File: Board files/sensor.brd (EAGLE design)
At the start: 25.4 x 59.7 mm, 32 parts, among them Q1 BCM847DS, U1 TL974, U2 TL974

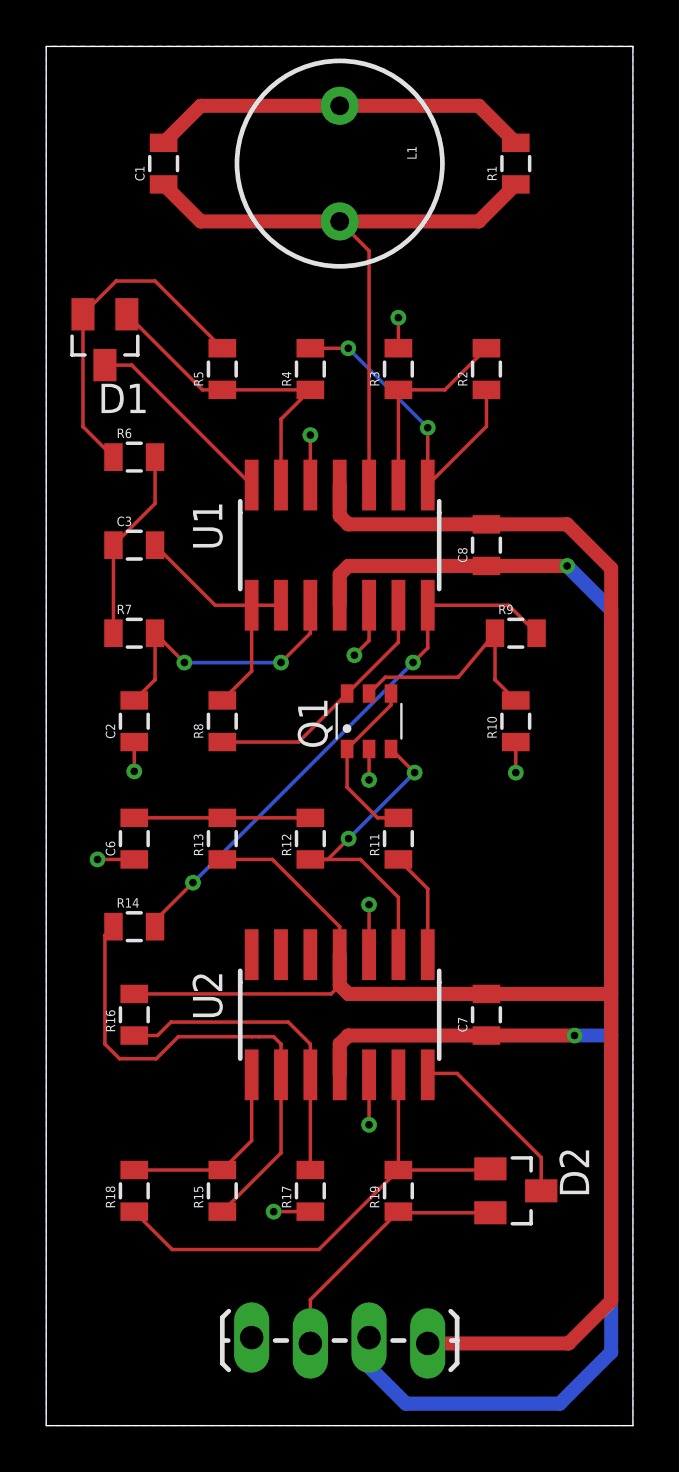
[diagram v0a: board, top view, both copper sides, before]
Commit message: Added component values and removed final rectifier
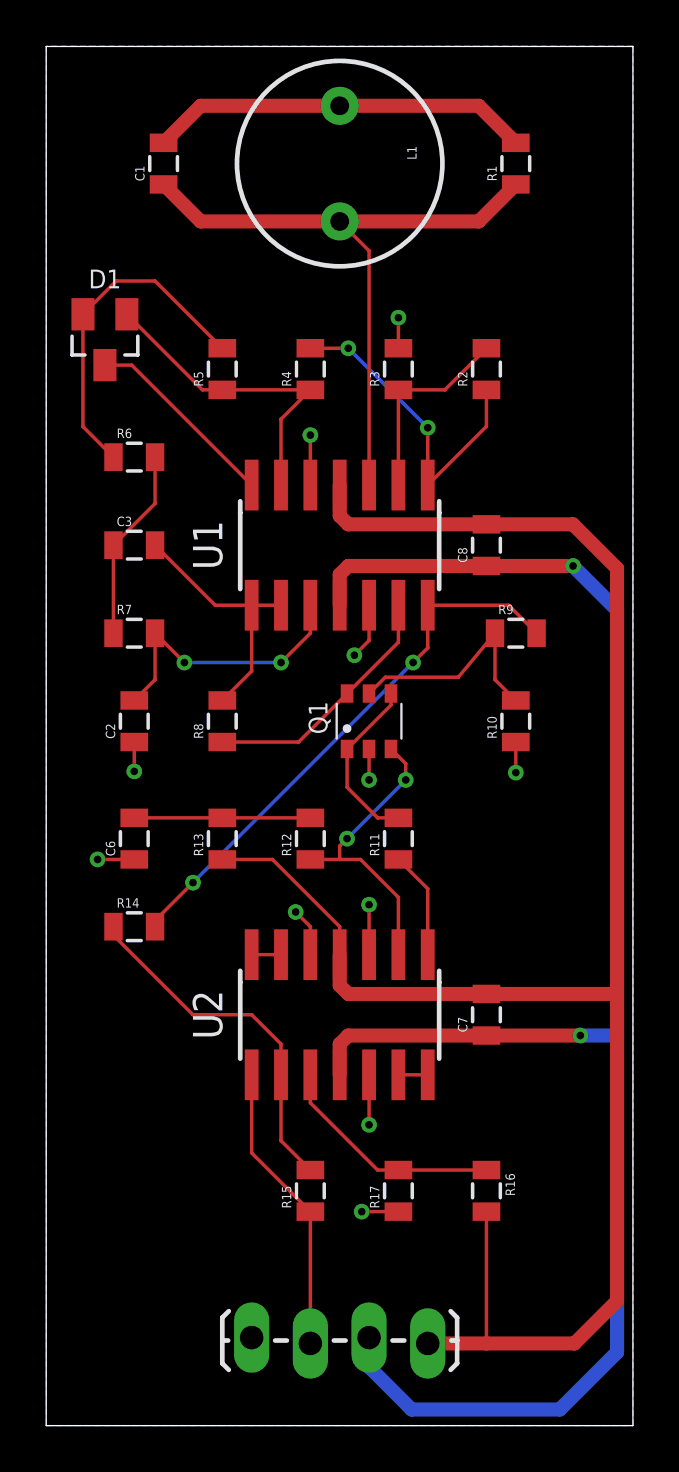
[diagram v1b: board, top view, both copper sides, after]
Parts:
- removed D2: BAS70-04, diode:SOT23
- removed R18, R19: (no value), SparkFun-Resistors:0805
- C1: value (none) -> 4.7nF
- C6: value (none) -> 0.1uF
- L1: value (none) -> 1mH
- R1, R10: value (none) -> 1K
- R11: value (none) -> 2K
- R12, R13: value (none) -> 499K
- R14, R17, R3, R4, R5, R8: value (none) -> 10K
- R15, R2: value (none) -> 68K
- R16: value (none) -> 40.2K
- R9: value (none) -> 15K
- moved R16 17.0 mm to (19.1, 10.2), turned to 270 degrees
- moved R17 3.81 mm to (15.2, 10.2)
- moved R15 3.81 mm to (11.4, 10.2)
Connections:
- removed net N$23: D2.1, R18.1, R19.2, U2.13
- removed net N$25: D2.3, U2.14
- removed net N$26: D2.2, JP1.2, R19.1
- new net N$11: U2.13, U2.14
- new net N$9: U2.6, U2.7
- net GND: now also U2.5
- net N$22: now also R15.2; no longer R15.1
- net N$24: now also JP1.2, R15.1; no longer R15.2, R18.2
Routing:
- net N$23: track 21.7 -> 0.00 mm
- net N$26: track 11.3 -> 0.00 mm
- net N$25: track 7.88 -> 0.00 mm
- net N$22: track 21.9 -> 15.5 mm
- net N$24: track 8.46 -> 12.7 mm
- net N$20: track 13.7 -> 10.0 mm
- net VCC: track 84.2 -> 81.6 mm
- net GND: track 33.9 -> 36.0 mm, vias 10 -> 11
- net N$19: track 14.5 -> 13.2 mm
- net N$11: track 0.00 -> 1.27 mm
- net N$9: track 0.00 -> 1.27 mm
- net VNEG: track 72.7 -> 73.7 mm

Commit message: Fixed decoupling caps and added labels
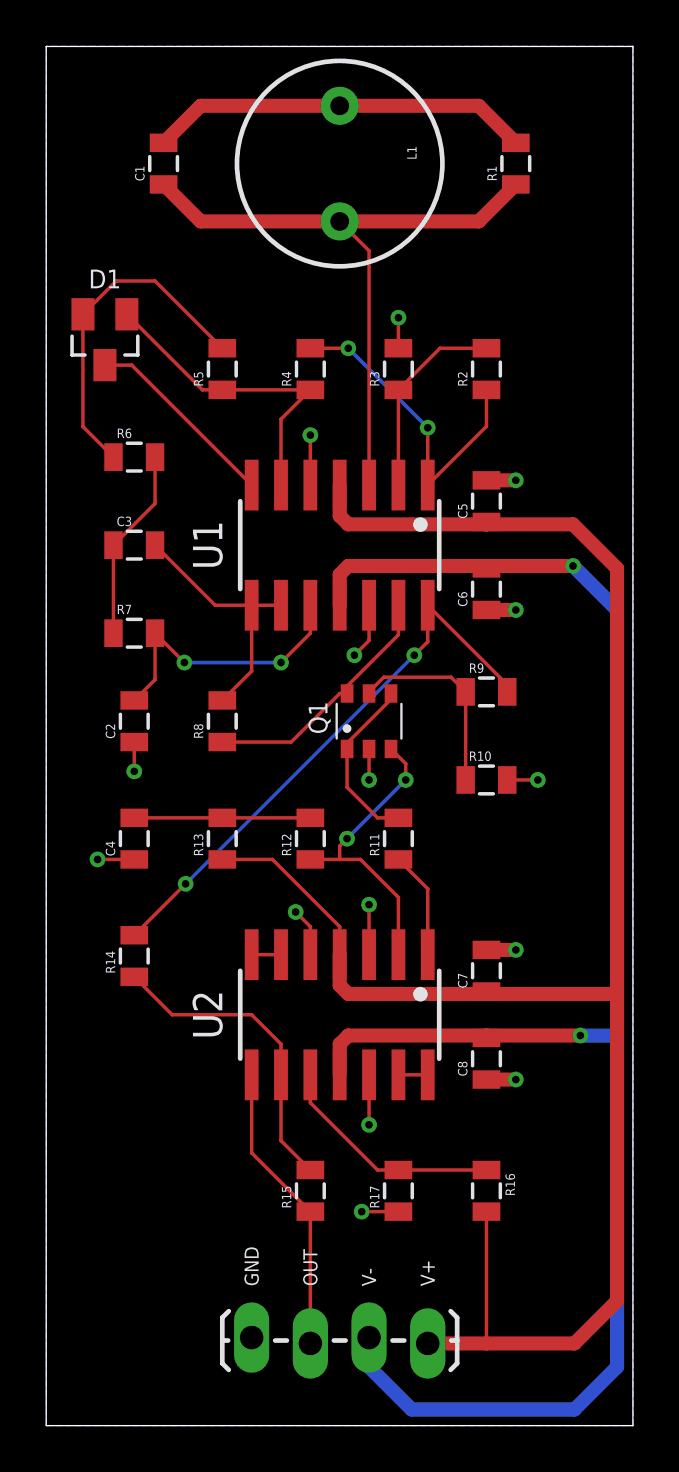
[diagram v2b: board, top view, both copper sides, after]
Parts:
- added C4, C5: 0.1uF, SparkFun-Capacitors:0805
- C7, C8: value 0.15uF -> 0.1uF
- moved C8 22.2 mm to (19.1, 15.9)
- moved C6 18.7 mm to (19.1, 36.2)
- moved R10 2.84 mm to (19.1, 27.9), turned to 0 degrees
- moved R9 2.84 mm to (19.1, 31.8)
- moved C7 1.90 mm to (19.1, 19.7)
- moved R14 1.27 mm to (3.81, 20.3), turned to 90 degrees
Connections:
- net GND: now also C4.1, C5.2, C7.2, C8.1, R10.2; no longer R10.1
- net N$16: now also R10.1; no longer R10.2
- net N$18: now also C4.2; no longer C6.2
- net VCC: now also C5.1, C7.1; no longer C7.2, C8.2
- net VNEG: now also C6.2, C8.2; no longer C7.1, C8.1
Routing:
- net GND: track 36.0 -> 41.1 mm, vias 11 -> 15
- net N$22: track 15.5 -> 13.5 mm
- net N$16: track 9.92 -> 8.59 mm
- net N$17: track 24.0 -> 24.7 mm
- net VNEG: track 73.7 -> 74.3 mm
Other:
- board text added: "GND"
- board text added: "OUT"
- board text added: "V+"
- board text added: "V-"

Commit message: Added larger decoupling capacitors to the sensor boards
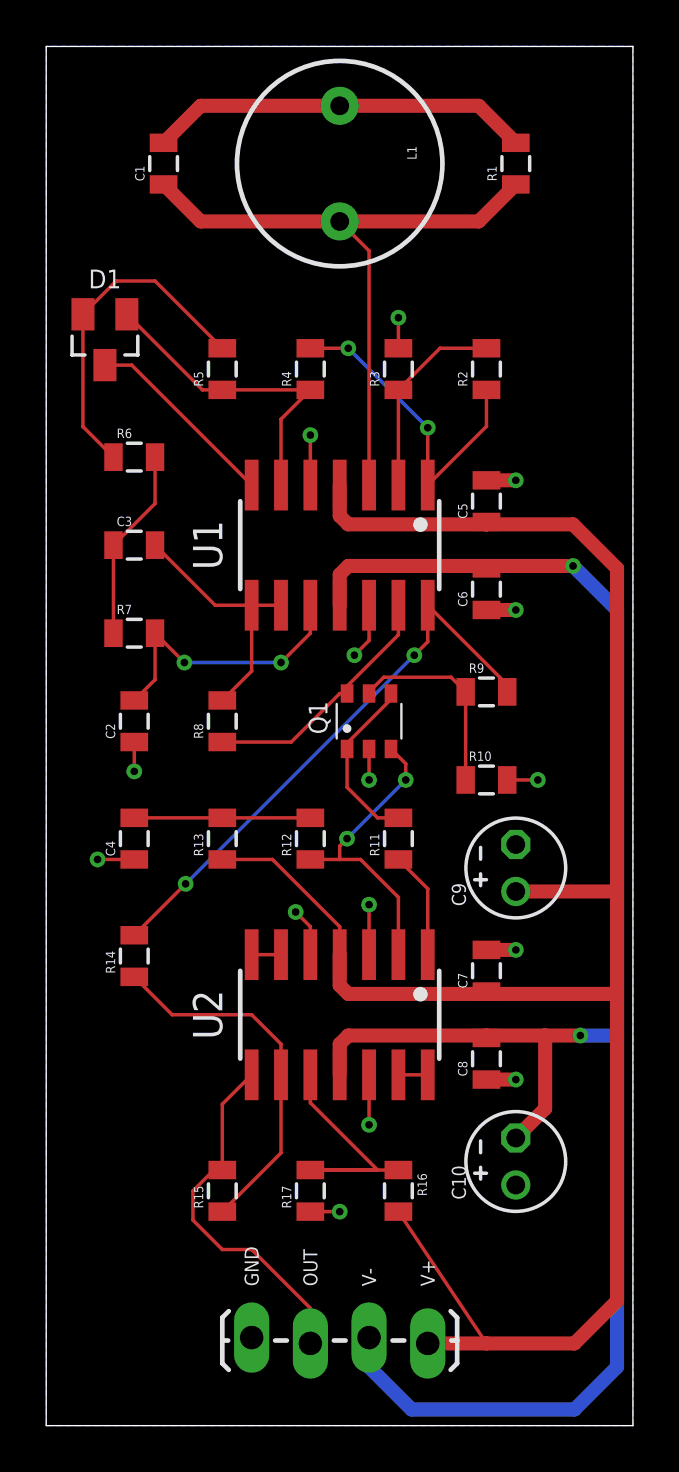
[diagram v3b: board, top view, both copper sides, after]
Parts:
- added C10, C9: (no value), resistor:E2-4
- moved R16 3.81 mm to (15.2, 10.2)
- moved R17 3.81 mm to (11.4, 10.2)
- moved R15 3.81 mm to (7.62, 10.2)
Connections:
- net GND: now also C10.+, C9.-
- net N$22: now also R15.1; no longer R15.2
- net N$24: now also R15.2; no longer R15.1
- net VCC: now also C9.+
- net VNEG: now also C10.-
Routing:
- net VCC: track 81.8 -> 87.4 mm
- net VNEG: track 74.3 -> 79.2 mm
- net N$24: track 12.7 -> 15.7 mm
- net N$22: track 13.5 -> 15.9 mm
- net N$20: track 10.0 -> 12.0 mm
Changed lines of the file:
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@@
 <element name="C4" library="SparkFun-Capacitors" package="0805" value="0.1uF" x="3.81" y="25.4" rot="R90"/>
 <element name="R14" library="SparkFun-Resistors" package="0805" value="10K" x="3.81" y="20.32" rot="R90"/>
-<element name="R15" library="SparkFun-Resistors" package="0805" value="68K" x="11.43" y="10.16" rot="R90"/>
-<element name="R16" library="SparkFun-Resistors" package="0805" value="40.2K" x="19.05" y="10.16" rot="R270"/>
-<element name="R17" library="SparkFun-Resistors" package="0805" value="10K" x="15.24" y="10.16" rot="R90"/>
+<element name="R15" library="SparkFun-Resistors" package="0805" value="68K" x="7.62" y="10.16" rot="R90"/>
+<element name="R16" library="SparkFun-Resistors" package="0805" value="40.2K" x="15.24" y="10.16" rot="R270"/>
+<element name="R17" library="SparkFun-Resistors" package="0805" value="10K" x="11.43" y="10.16" rot="R90"/>
 <element name="C7" library="SparkFun-Capacitors" package="0805" value="0.1uF" x="19.05" y="19.685" rot="R90"/>
 <element name="C8" library="SparkFun-Capacitors" package="0805" value="0.1uF" x="19.05" y="15.875" rot="R90"/>
 <element name="C5" library="SparkFun-Capacitors" package="0805" value="0.1uF" x="19.05" y="40.005" rot="R90"/>
 <element name="C6" library="SparkFun-Capacitors" package="0805" value="0.1uF" x="19.05" y="36.195" rot="R90"/>
+<element name="C9" library="resistor" package="E2-4" value="" x="20.32" y="24.13" smashed="yes" rot="R90">
+<attribute name="NAME" x="18.161" y="22.479" size="0.6096" layer="25" rot="R90"/>
+<attribute name="VALUE" x="22.479" y="26.289" size="1.27" layer="27" ratio="10" rot="R90"/>
+</element>
+<element name="C10" library="resistor" package="E2-4" value="" x="20.32" y="11.43" smashed="yes" rot="R90">
+<attribute name="NAME" x="18.161" y="9.779" size="0.6096" layer="25" rot="R90"/>
+<attribute name="VALUE" x="22.479" y="13.589" size="1.27" layer="27" ratio="10" rot="R90"/>
+</element>
 </elements>
 <signals>
@@
 <wire x1="13.97" y1="20.38" x2="13.97" y2="22.5425" width="0.1524" layer="1"/>
 <via x="13.97" y="22.5425" extent="1-16" drill="0.3302"/>
-<wire x1="15.24" y1="9.26" x2="13.6525" y2="9.26" width="0.1524" layer="1"/>
-<via x="13.6525" y="9.26" extent="1-16" drill="0.3302"/>
+<wire x1="11.43" y1="9.26" x2="12.7" y2="9.26" width="0.1524" layer="1"/>
+<via x="12.7" y="9.26" extent="1-16" drill="0.3302"/>
 <wire x1="13.97" y1="35.5" x2="13.97" y2="33.9725" width="0.1524" layer="1"/>
 <wire x1="13.97" y1="33.9725" x2="13.335" y2="33.3375" width="0.1524" layer="1"/>
@@
 <wire x1="19.05" y1="14.975" x2="20.32" y2="14.975" width="0.6096" layer="1"/>
 <via x="20.32" y="14.975" extent="1-16" drill="0.3302"/>
+<contactref element="C9" pad="-"/>
+<contactref element="C10" pad="+"/>
 </signal>
 <signal name="VCC">
@@
 <wire x1="22.86" y1="3.556" x2="24.7015" y2="5.3975" width="0.6096" layer="1"/>
 <wire x1="24.7015" y1="5.3975" x2="24.7015" y2="18.68" width="0.6096" layer="1"/>
-<wire x1="24.7015" y1="19.05" x2="24.7015" y2="37.095" width="0.6096" layer="1"/>
+<wire x1="24.7015" y1="18.68" x2="24.7015" y2="22.86" width="0.6096" layer="1"/>
+<wire x1="24.7015" y1="23.114" x2="24.7015" y2="37.095" width="0.6096" layer="1"/>
 <wire x1="24.7015" y1="37.095" x2="22.7965" y2="39" width="0.6096" layer="1"/>
 <wire x1="7.62" y1="24.5" x2="9.79" y2="24.5" width="0.1524" layer="1"/>
@@
 <wire x1="13.07" y1="39" x2="12.7" y2="39.37" width="0.6096" layer="1"/>
 <wire x1="12.7" y1="39.37" x2="12.7" y2="40.7" width="0.6096" layer="1"/>
-<wire x1="19.05" y1="9.26" x2="19.05" y2="3.556" width="0.1524" layer="1"/>
+<wire x1="15.24" y1="9.26" x2="19.05" y2="3.556" width="0.1524" layer="1"/>
 <contactref element="C5" pad="1"/>
 <contactref element="C7" pad="1"/>
@@
 <wire x1="19.05" y1="18.68" x2="19.05" y2="18.785" width="0.6096" layer="1"/>
 <wire x1="19.05" y1="18.68" x2="24.7015" y2="18.68" width="0.6096" layer="1"/>
-<wire x1="24.7015" y1="18.68" x2="24.7015" y2="19.05" width="0.6096" layer="1"/>
+<contactref element="C9" pad="+"/>
+<wire x1="20.32" y1="23.114" x2="24.7015" y2="23.114" width="0.6096" layer="1"/>
+<wire x1="24.7015" y1="23.114" x2="24.7015" y2="22.86" width="0.6096" layer="1"/>
 </signal>
 <signal name="N$3">
@@
 <wire x1="19.05" y1="37.2" x2="19.05" y2="37.095" width="0.6096" layer="1"/>
 <wire x1="13.07" y1="16.88" x2="19.05" y2="16.88" width="0.6096" layer="1"/>
-<wire x1="23.114" y1="16.88" x2="19.05" y2="16.88" width="0.6096" layer="1"/>
+<wire x1="23.114" y1="16.88" x2="21.59" y2="16.88" width="0.6096" layer="1"/>
+<wire x1="21.59" y1="16.88" x2="19.05" y2="16.88" width="0.6096" layer="1"/>
 <wire x1="19.05" y1="16.88" x2="19.05" y2="16.775" width="0.6096" layer="1"/>
+<contactref element="C10" pad="-"/>
+<wire x1="21.59" y1="13.716" x2="21.59" y2="16.88" width="0.6096" layer="1"/>
+<wire x1="20.32" y1="12.446" x2="21.59" y2="13.716" width="0.6096" layer="1"/>
 </signal>
 <signal name="N$2">
@@
 <wire x1="11.43" y1="15.18" x2="11.43" y2="13.97" width="0.1524" layer="1"/>
 <wire x1="11.43" y1="13.97" x2="14.34" y2="11.06" width="0.1524" layer="1"/>
-<wire x1="14.34" y1="11.06" x2="15.24" y2="11.06" width="0.1524" layer="1"/>
-<wire x1="15.24" y1="11.06" x2="19.05" y2="11.06" width="0.1524" layer="1"/>
+<wire x1="14.34" y1="11.06" x2="11.43" y2="11.06" width="0.1524" layer="1"/>
+<wire x1="11.43" y1="11.06" x2="15.24" y2="11.06" width="0.1524" layer="1"/>
 </signal>
 <signal name="N$22">
 <contactref element="R14" pad="1"/>
 <contactref element="U2" pad="9"/>
-<contactref element="R15" pad="2"/>
-<wire x1="10.16" y1="15.18" x2="10.16" y2="12.33" width="0.1524" layer="1"/>
-<wire x1="10.16" y1="12.33" x2="11.43" y2="11.06" width="0.1524" layer="1"/>
+<contactref element="R15" pad="1"/>
 <wire x1="5.45" y1="17.78" x2="8.89" y2="17.78" width="0.1524" layer="1"/>
 <wire x1="8.89" y1="17.78" x2="10.16" y2="16.51" width="0.1524" layer="1"/>
 <wire x1="10.16" y1="16.51" x2="10.16" y2="15.18" width="0.1524" layer="1"/>
 <wire x1="3.81" y1="19.42" x2="5.45" y2="17.78" width="0.1524" layer="1"/>
+<wire x1="10.16" y1="15.18" x2="10.16" y2="11.8" width="0.1524" layer="1"/>
+<wire x1="10.16" y1="11.8" x2="7.62" y2="9.26" width="0.1524" layer="1"/>
 </signal>
 <signal name="N$24">
 <contactref element="U2" pad="8"/>
-<contactref element="R15" pad="1"/>
+<contactref element="R15" pad="2"/>
 <contactref element="JP1" pad="2"/>
-<wire x1="8.89" y1="15.18" x2="8.89" y2="11.8" width="0.1524" layer="1"/>
-<wire x1="8.89" y1="11.8" x2="11.43" y2="9.26" width="0.1524" layer="1"/>
-<wire x1="11.43" y1="9.26" x2="11.43" y2="3.556" width="0.1524" layer="1"/>
+<wire x1="8.89" y1="15.18" x2="7.62" y2="13.91" width="0.1524" layer="1"/>
+<wire x1="7.62" y1="13.91" x2="7.62" y2="11.06" width="0.1524" layer="1"/>
+<wire x1="7.62" y1="11.06" x2="7.25" y2="11.06" width="0.1524" layer="1"/>
+<wire x1="7.25" y1="11.06" x2="6.35" y2="10.16" width="0.1524" layer="1"/>
+<wire x1="6.35" y1="10.16" x2="6.35" y2="8.89" width="0.1524" layer="1"/>
+<wire x1="6.35" y1="8.89" x2="7.62" y2="7.62" width="0.1524" layer="1"/>
+<wire x1="7.62" y1="7.62" x2="8.89" y2="7.62" width="0.1524" layer="1"/>
+<wire x1="8.89" y1="7.62" x2="11.43" y2="5.08" width="0.1524" layer="1"/>
+<wire x1="11.43" y1="5.08" x2="11.43" y2="3.556" width="0.1524" layer="1"/>
 </signal>
 <signal name="N$9">

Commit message: Increased initial sensor gain from 8 to 256
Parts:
- C10, C9: value (none) -> 10uF
- R2: value 68K -> 15K
- R3, R4: value 10K -> 1K
- R5: value 10K -> 15K
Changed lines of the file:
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@@
 <element name="R1" library="SparkFun-Resistors" package="0805" value="1K" x="20.32" y="54.61" rot="R90"/>
 <element name="C1" library="SparkFun-Capacitors" package="0805" value="4.7nF" x="5.08" y="54.61" rot="R90"/>
-<element name="R2" library="SparkFun-Resistors" package="0805" value="68K" x="19.05" y="45.72" rot="R90"/>
-<element name="R3" library="SparkFun-Resistors" package="0805" value="10K" x="15.24" y="45.72" rot="R90"/>
-<element name="R4" library="SparkFun-Resistors" package="0805" value="10K" x="11.43" y="45.72" rot="R90"/>
-<element name="R5" library="SparkFun-Resistors" package="0805" value="10K" x="7.62" y="45.72" rot="R90"/>
+<element name="R2" library="SparkFun-Resistors" package="0805" value="15K" x="19.05" y="45.72" rot="R90"/>
+<element name="R3" library="SparkFun-Resistors" package="0805" value="1K" x="15.24" y="45.72" rot="R90"/>
+<element name="R4" library="SparkFun-Resistors" package="0805" value="1K" x="11.43" y="45.72" rot="R90"/>
+<element name="R5" library="SparkFun-Resistors" package="0805" value="15K" x="7.62" y="45.72" rot="R90"/>
 <element name="R6" library="SparkFun-Resistors" package="0805" value="10K" x="3.81" y="41.91"/>
 <element name="C2" library="SparkFun-Capacitors" package="0805" value="0.1uF" x="3.81" y="30.48" rot="R90"/>
@@
 <element name="C5" library="SparkFun-Capacitors" package="0805" value="0.1uF" x="19.05" y="40.005" rot="R90"/>
 <element name="C6" library="SparkFun-Capacitors" package="0805" value="0.1uF" x="19.05" y="36.195" rot="R90"/>
-<element name="C9" library="resistor" package="E2-4" value="" x="20.32" y="24.13" smashed="yes" rot="R90">
+<element name="C9" library="resistor" package="E2-4" value="10uF" x="20.32" y="24.13" smashed="yes" rot="R90">
 <attribute name="NAME" x="18.161" y="22.479" size="0.6096" layer="25" rot="R90"/>
 <attribute name="VALUE" x="22.479" y="26.289" size="1.27" layer="27" ratio="10" rot="R90"/>
 </element>
-<element name="C10" library="resistor" package="E2-4" value="" x="20.32" y="11.43" smashed="yes" rot="R90">
+<element name="C10" library="resistor" package="E2-4" value="10uF" x="20.32" y="11.43" smashed="yes" rot="R90">
 <attribute name="NAME" x="18.161" y="9.779" size="0.6096" layer="25" rot="R90"/>
 <attribute name="VALUE" x="22.479" y="13.589" size="1.27" layer="27" ratio="10" rot="R90"/>
